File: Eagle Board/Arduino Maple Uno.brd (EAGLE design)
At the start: 68.6 x 53.6 mm, 66 parts, among them T1 BC847, T2 BC847, U1 3.3V, U2 MCP9808MSOP, X1 8Mhz

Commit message: changes in design
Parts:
- removed U$4: 3015-INDUCTOR, LCSC:3015
- added C13: 100nF, resistor:C0603
- added U$6: 6045-3.6A-INDUCTOR, LCSC:INDC6161X450
- R11: value 56k -> 100k
- R12: value 10k -> 13.7k
- T1, T2: value BC847 -> S8050
- U$2: value ME3116 -> SY8113
- moved C16 9.03 mm to (25.9, 23.5)
- moved C15 9.00 mm to (23.7, 23.1)
- moved U1 7.96 mm to (18.7, 26.2)
- moved C5 0.46 mm to (53.8, 24.6)
- moved C8 0.46 mm to (10.3, 31.4)
- moved C7 0.38 mm to (9.65, 41.0)
- moved D1 0.36 mm to (6.86, 30.6)
- moved R18 0.25 mm to (6.35, 43.9)
- moved J1 0.13 mm to (1.91, 38.4)
- moved R11 0.13 mm to (4.19, 21.6)
- moved R12 0.13 mm to (2.03, 21.6)
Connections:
- net 3.3V: now also C13.1; no longer LED2.A
- net 33: now also LED2.A; no longer R23.2
- net GND: now also C13.2, R23.2
- net N$24: now also U$6.2; no longer U$4.2
- net N$5: now also U$6.1; no longer U$4.1
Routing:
- net 3.3V: track 182.3 -> 164.5 mm
- net VBUS: track 21.3 -> 19.8 mm
- net 5V: track 46.0 -> 44.8 mm
- net RESET: track 130.6 -> 129.6 mm
- net 5: track 22.5 -> 23.3 mm
- net 33: track 22.7 -> 23.5 mm
- net N$13: track 12.5 -> 12.0 mm
- net GND: track 4.06 -> 4.12 mm, vias 63 -> 82
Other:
- board text added: "Made in Vietnam"

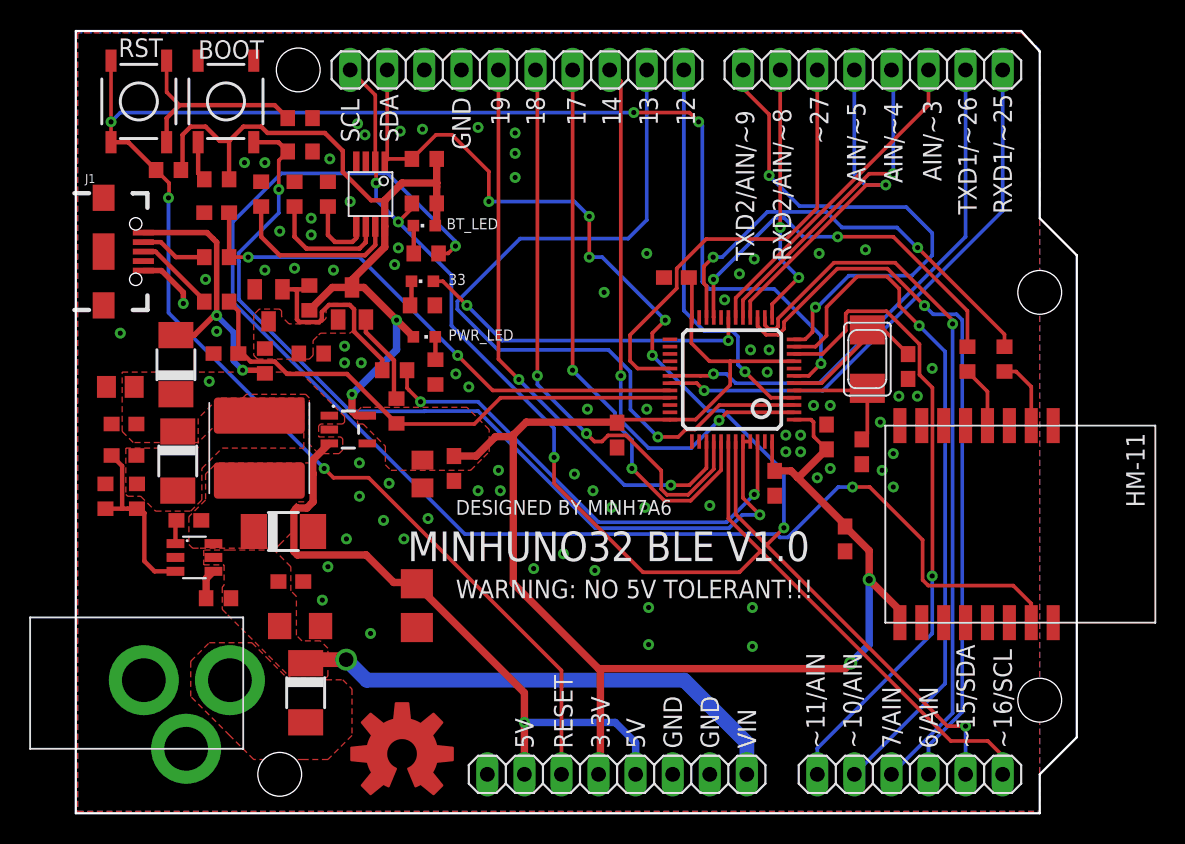
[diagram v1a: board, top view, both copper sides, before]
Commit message: added MPU6050 IMU
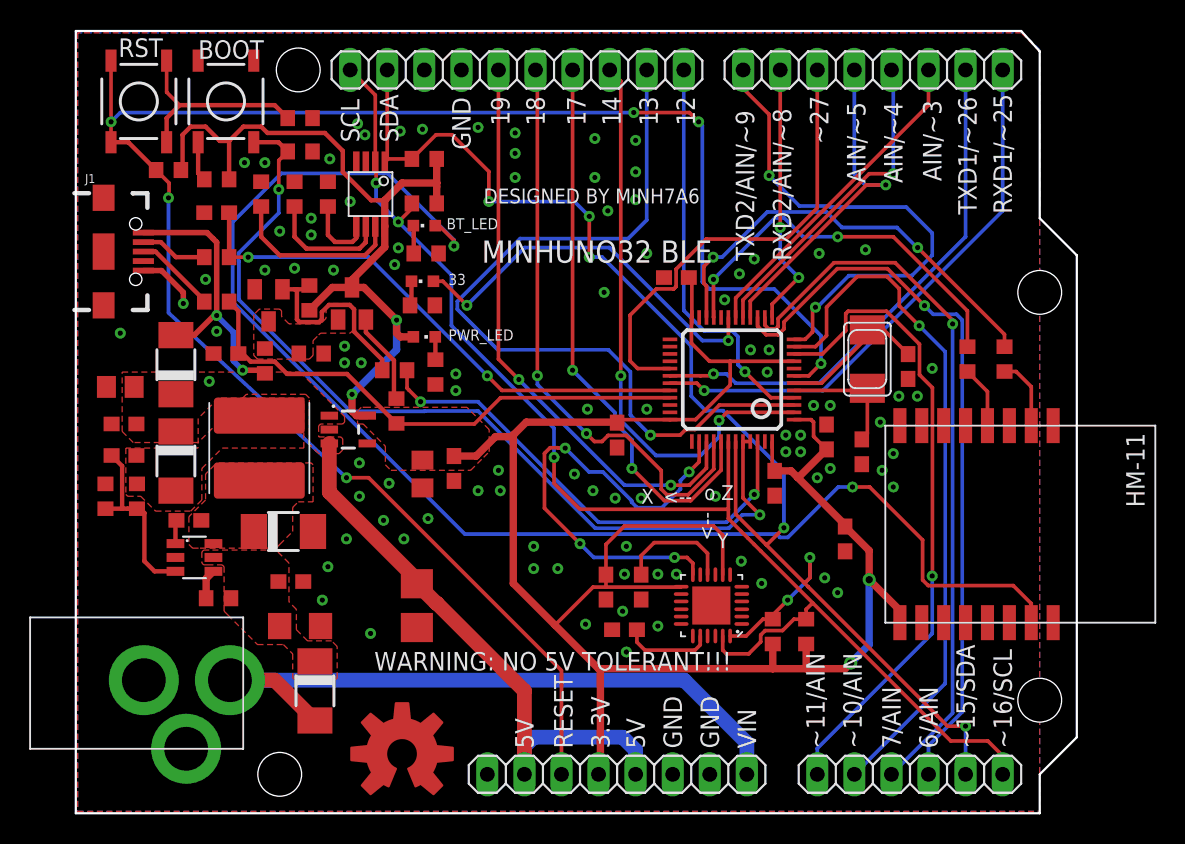
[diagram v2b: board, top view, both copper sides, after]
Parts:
- added C19: 10nF, resistor:C0603
- added C20: 2.2nF, resistor:C0603
- added C21: 100nF, resistor:C0603
- added R25, R26: 10k, resistor:R0603
- added U$4: MPU-6050-1, LCSC:TESTING_QFN-24-4MM2
- moved D3 0.65 mm to (16.4, 8.26)
- moved D4 0.13 mm to (6.86, 24.0)
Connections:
- new net N$33: C21.1, U$4.10
- new net N$35: C20.1, U$4.20
- net 20: now also U$4.12
- net 3.3V: now also C19.1, R25.2, R26.2, U$4.13, U$4.8; no longer LED1.A
- net GND: now also C19.2, C20.2, C21.2, R22.2, U$4.1, U$4.11, U$4.18, U$4.9
- net N$20: now also C12.1, C17.1, D3.C, R10.2, U$2.5; no longer D3.A, U$3.TIP
- net PIO1: now also LED1.A; no longer R22.2
- net SCL: now also R25.1, U$4.23
- net SDA: now also R26.1, U$4.24
- net VIN: now also D3.A, U$3.TIP; no longer C12.1, C17.1, D3.C, R10.2, U$2.5
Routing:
- net 20: track 0.00 -> 31.8 mm, vias 0 -> 4
- net 3.3V: track 164.5 -> 190.7 mm
- net VIN: track 34.8 -> 46.3 mm, vias 1 -> 0
- net SDA: track 85.1 -> 95.1 mm
- net N$33: track 0.00 -> 7.99 mm
- net N$35: track 0.00 -> 6.17 mm
- net SCL: track 85.1 -> 89.9 mm
- net 5V: track 44.8 -> 40.1 mm, vias 1 -> 0
- net 33: track 23.5 -> 26.8 mm
- net 14: track 38.0 -> 39.1 mm
- net 27: track 31.4 -> 32.1 mm
- net PIO1: track 94.8 -> 95.5 mm
- net GND: vias 82 -> 96
- removed copper zone on layer 1, net VIN
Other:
- board text added: "<--"
- board text added: "MINHUNO32 BLE"
- board text added: "X"
- board text added: "Y"
- board text added: "o Z"
- board text removed: "MINHUNO32 BLE V1.0"
